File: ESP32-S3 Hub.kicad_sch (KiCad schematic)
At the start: 21 parts, among them U1 ESP32-S3 FN8, Y1 ABM11-40.000MHZ-B1U-T3, 10ppm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

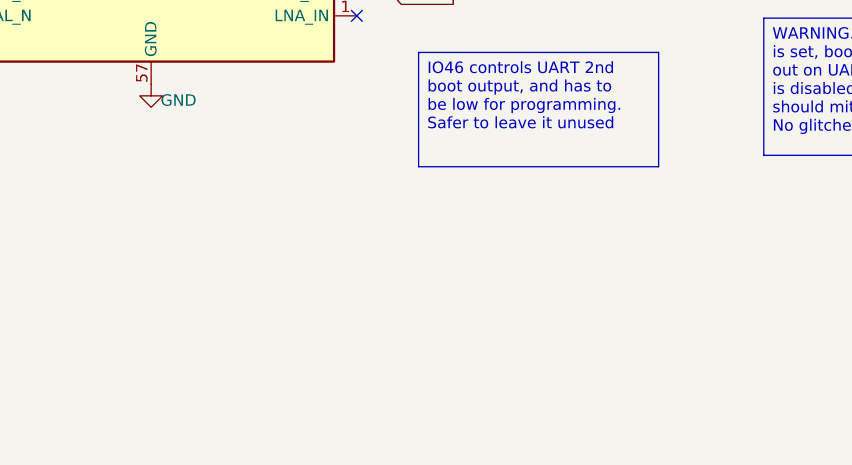
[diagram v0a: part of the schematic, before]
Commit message: Fixed typos with ADC-4 pins, split a few circuits
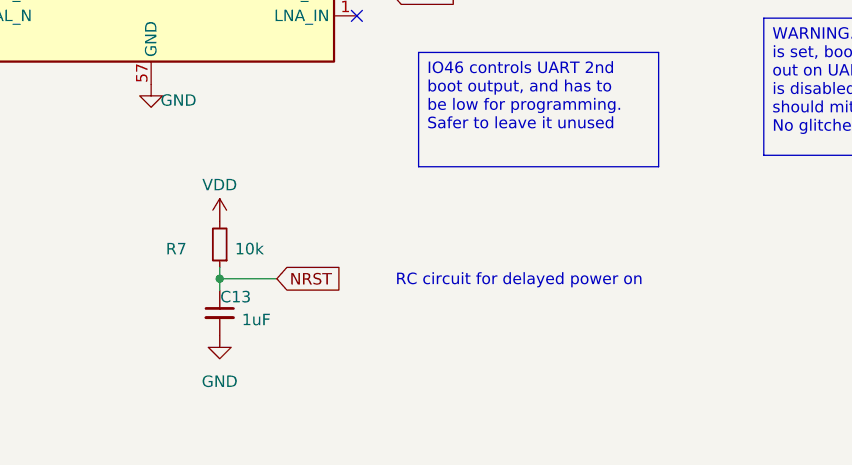
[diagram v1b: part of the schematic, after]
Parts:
- added C13: 1uF, Capacitor_SMD:C_0402_1005Metric, symbol Device:C_Small
- added R7: 10k, Resistor_SMD:R_0402_1005Metric, symbol Device:R_Small
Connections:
- net GND: now also C13.2
- net NRST: now also C13.1, R7.1
- net VDD: now also R7.2
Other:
- note added: "RC circuit for delayed power on"

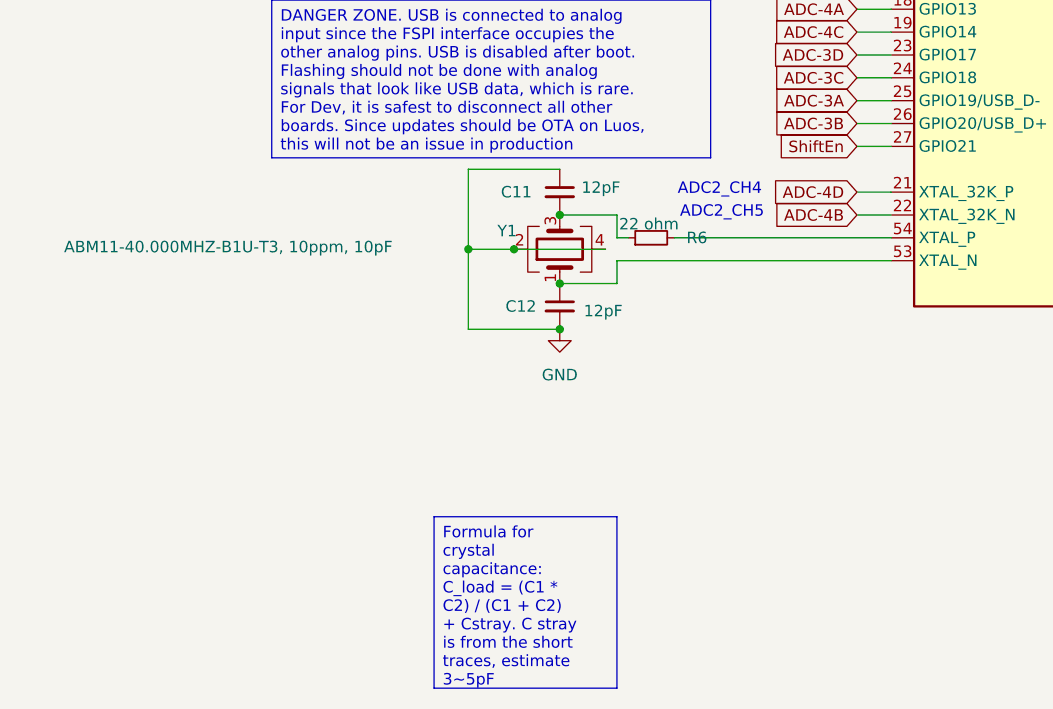
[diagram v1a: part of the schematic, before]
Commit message: Changed clock schematic layout
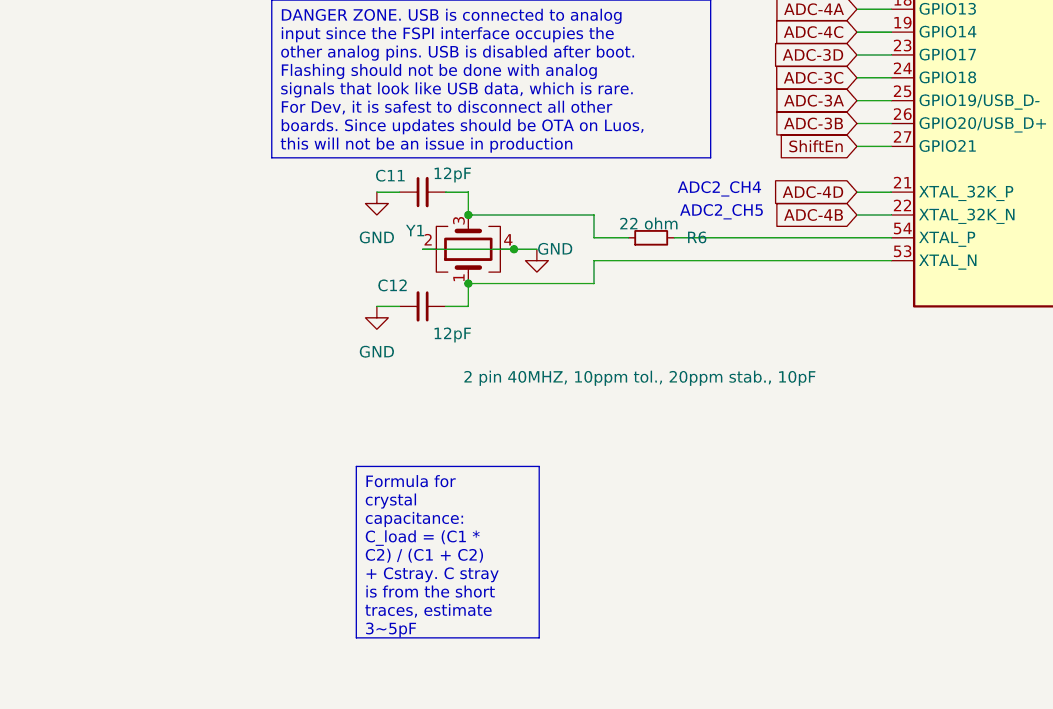
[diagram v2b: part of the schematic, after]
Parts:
- Y1: value ABM11-40.000MHZ-B1U-T3, 10ppm, 10pF -> 2 pin 40MHZ, 10ppm tol., 20ppm stab., 10pF
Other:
- moved on the sheet: C11, C12, Y1

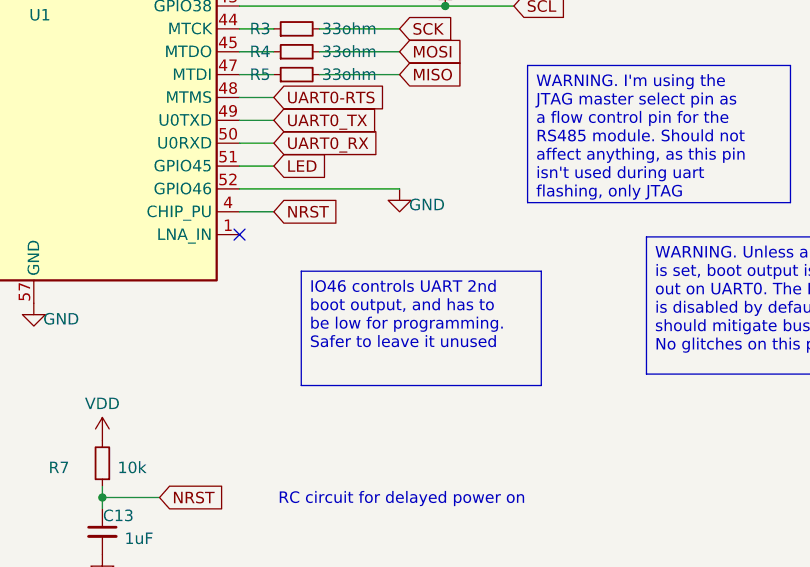
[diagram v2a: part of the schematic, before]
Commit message: Changed configurable resistor pin in schematic
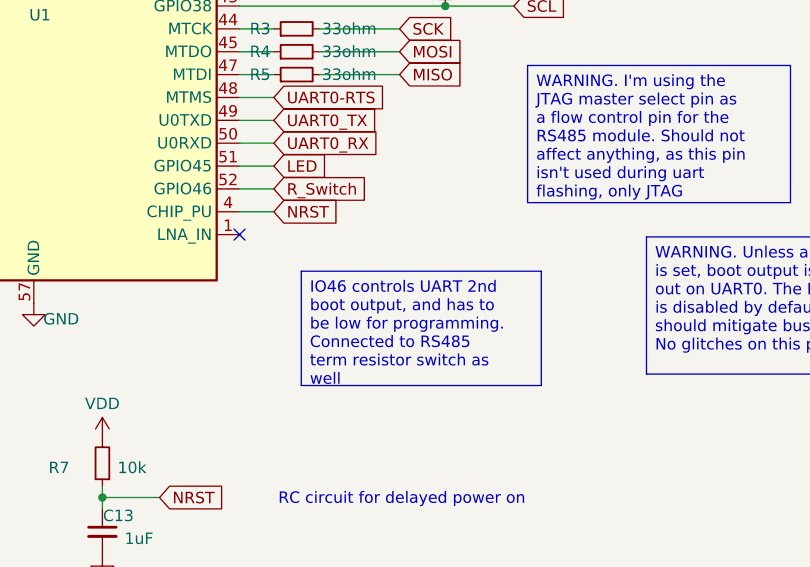
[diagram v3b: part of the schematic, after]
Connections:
- net GND: no longer U1.52 (GPIO46)
- new net R_Switch: U1.52 (GPIO46)
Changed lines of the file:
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@@
 		)
 	)
-	(text_box "IO46 controls UART 2nd boot output, and has to be low for programming. Safer to leave it unused"
+	(text_box "IO46 controls UART 2nd boot output, and has to be low for programming. Connected to RS485 term resistor switch as well"
 		(exclude_from_sim no)
 		(at 174.498 127.254 0)
@@
 	(wire
 		(pts
-			(xy 167.64 118.11) (xy 185.42 118.11)
+			(xy 167.64 118.11) (xy 171.45 118.11)
 		)
 		(stroke
@@
 		)
 	)
+	(global_label "R_Switch"
+		(shape input)
+		(at 171.45 118.11 0)
+		(fields_autoplaced yes)
+		(effects
+			(font
+				(size 1.27 1.27)
+			)
+			(justify left)
+		)
+		(property "Intersheetrefs" "${INTERSHEET_REFS}"
+			(at 182.7809 118.11 0)
+			(effects
+				(font
+					(size 1.27 1.27)
+				)
+				(justify left)
+				(hide yes)
+			)
+		)
+	)
 	(global_label "CS-3"
 		(shape input)
@@
 					(unit 1)
 				)
-			)
-		)
-	)
-	(symbol
-		(lib_id "power:GND")
-		(at 185.42 118.11 0)
-		(unit 1)
-		(exclude_from_sim no)
-		(in_bom yes)
-		(on_board yes)
-		(dnp no)
-		(property "Reference" "#PWR043"
-			(at 185.42 124.46 0)
-			(effects
-				(font
-					(size 1.27 1.27)
-				)
-				(hide yes)
-			)
-		)
-		(property "Value" "GND"
-			(at 188.468 119.888 0)
-			(effects
-				(font
-					(size 1.27 1.27)
-				)
-			)
-		)
-		(property "Footprint" ""
-			(at 185.42 118.11 0)
-			(effects
-				(font
-					(size 1.27 1.27)
-				)
-				(hide yes)
-			)
-		)
-		(property "Datasheet" ""
-			(at 185.42 118.11 0)
-			(effects
-				(font
-					(size 1.27 1.27)
-				)
-				(hide yes)
-			)
-		)
-		(property "Description" "Power symbol creates a global label with name \"GND\" , ground"
-			(at 185.42 118.11 0)
-			(effects
-				(font
-					(size 1.27 1.27)
-				)
-				(hide yes)
-			)
-		)
-		(pin "1"
-		)
-		(instances
-			(project "ESP32-S3 Hub"
-				(path "/a8c80fba-3bca-4358-b5bb-9ebf9383c658"
-					(reference "#PWR043")
-					(unit 1)
-				)

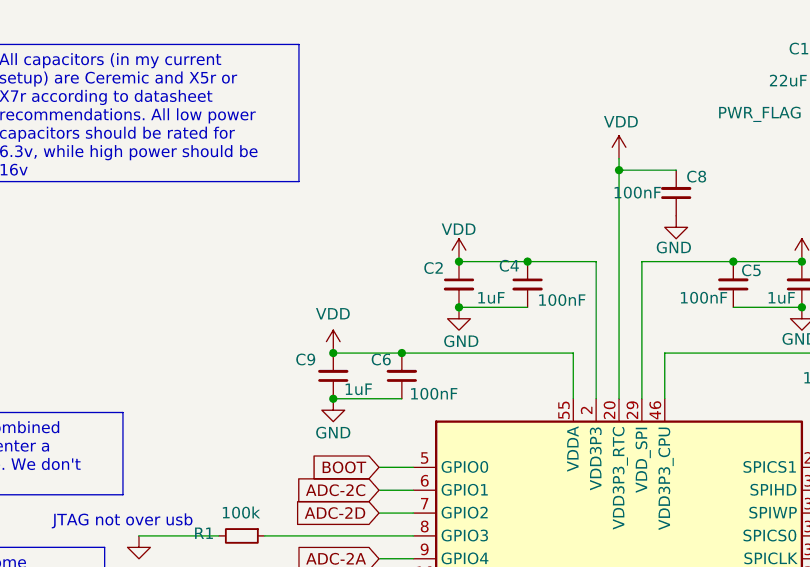
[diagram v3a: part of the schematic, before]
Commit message: Added 1 more bulk decop capacitor
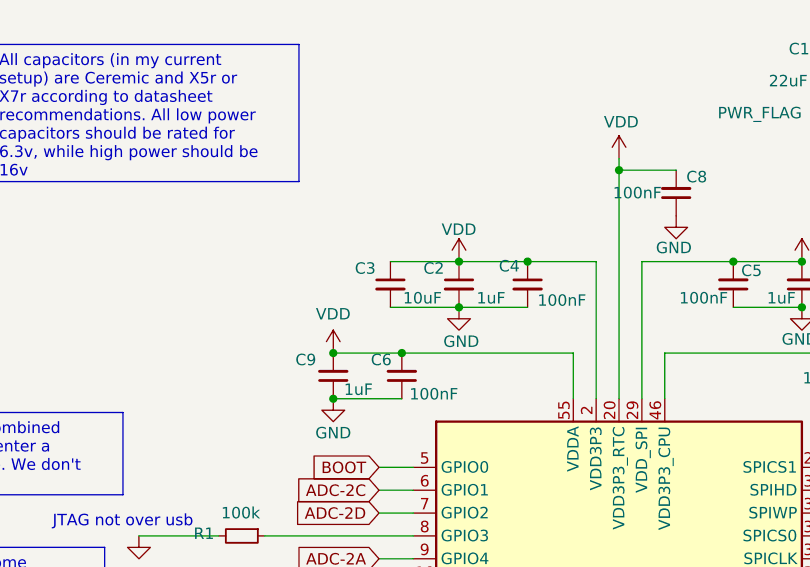
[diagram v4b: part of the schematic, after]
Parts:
- added C3: 10uF, Capacitor_SMD:C_0402_1005Metric, symbol Device:C_Small
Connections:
- net GND: now also C3.2
- net VDD: now also C3.1
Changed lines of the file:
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@@
+	(wire
+		(pts
+			(xy 119.38 44.45) (xy 127 44.45)
+		)
+		(stroke
+			(width 0)
+			(type default)
+		)
+	)
 	(wire
 		(pts
@@
 		(pts
 			(xy 171.45 22.86) (xy 173.99 22.86)
+		)
+		(stroke
+			(width 0)
+			(type default)
+		)
+	)
+	(wire
+		(pts
+			(xy 119.38 39.37) (xy 127 39.37)
 		)
 		(stroke
@@
 					(unit 1)
 				)
+			)
+		)
+	)
+	(symbol
+		(lib_id "Device:C_Small")
+		(at 119.38 41.91 0)
+		(unit 1)
+		(exclude_from_sim no)
+		(in_bom yes)
+		(on_board yes)
+		(dnp no)
+		(property "Reference" "C3"
+			(at 116.586 40.132 0)
+			(effects
+				(font
+					(size 1.27 1.27)
+				)
+			)
+		)
+		(property "Value" "10uF"
+			(at 122.936 43.434 0)
+			(effects
+				(font
+					(size 1.27 1.27)
+				)
+			)
+		)
+		(property "Footprint" "Capacitor_SMD:C_0402_1005Metric"
+			(at 119.38 41.91 0)
+			(effects
+				(font
+					(size 1.27 1.27)
+				)
+				(hide yes)
+			)
+		)
+		(property "Datasheet" "~"
+			(at 119.38 41.91 0)
+			(effects
+				(font
+					(size 1.27 1.27)
+				)
+				(hide yes)
+			)
+		)
+		(property "Description" "Unpolarized capacitor, small symbol"
+			(at 119.38 41.91 0)
+			(effects
+				(font
+					(size 1.27 1.27)
+				)
+				(hide yes)
+			)
+		)
+		(property "LCSC" "C52923"
+			(at 121.92 42.672 0)
+			(effects
+				(font
+					(size 1.27 1.27)
+				)
+				(hide yes)
+			)
+		)
+		(pin "2"
+		)
+		(pin "1"
+		)
+		(instances
+			(project "ESP32-S3 Hub"
+				(path "/a8c80fba-3bca-4358-b5bb-9ebf9383c658"
+					(reference "C3")
+					(unit 1)
+				)

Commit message: Fixed BOM LCSC part numbers mostly
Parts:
- C3: LCSC C52923 -> C15525
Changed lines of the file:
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@@
 			)
 		)
-		(property "LCSC" "C52923"
+		(property "LCSC" "C15525"
 			(at 121.92 42.672 0)
 			(effects

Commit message: Fixed clock to be on top only, moved to 0201, separate clock signals
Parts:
- C11, C12: footprint Capacitor_SMD:C_0402_1005Metric -> Capacitor_SMD:C_0201_0603Metric; LCSC C1547 -> C384960
- R6: footprint Resistor_SMD:R_0402_1005Metric -> Resistor_SMD:R_0201_0603Metric; LCSC C25092 -> C155743
- Y1: footprint Crystal:Crystal_SMD_2016-4Pin_2.0x1.6mm -> custom_Crystal:Crystal_SMD_1612-4Pin_1.6x1.2mm; LCSC C648973 -> C49158191
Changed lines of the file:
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@@
 			)
 		)
-		(property "Footprint" "Crystal:Crystal_SMD_2016-4Pin_2.0x1.6mm"
+		(property "Footprint" "custom_Crystal:Crystal_SMD_1612-4Pin_1.6x1.2mm"
 			(at 74.93 121.92 0)
 			(effects
@@
 			)
 		)
-		(property "LCSC" "C648973"
+		(property "LCSC" "C49158191"
 			(at 76.2 122.428 0)
 			(effects
@@
 			)
 		)
-		(property "Footprint" "Capacitor_SMD:C_0402_1005Metric"
+		(property "Footprint" "Capacitor_SMD:C_0201_0603Metric"
 			(at 69.85 128.27 0)
 			(effects
@@
 			)
 		)
-		(property "LCSC" "C1547"
+		(property "LCSC" "C384960"
 			(at 68.834 128.016 0)
 			(effects
@@
 			)
 		)
-		(property "Footprint" "Resistor_SMD:R_0402_1005Metric"
+		(property "Footprint" "Resistor_SMD:R_0201_0603Metric"
 			(at 95.25 120.65 0)
 			(effects
@@
 			)
 		)
-		(property "LCSC" "C25092"
+		(property "LCSC" "C155743"
 			(at 93.218 121.92 0)
 			(effects
@@
 			)
 		)
-		(property "Footprint" "Capacitor_SMD:C_0402_1005Metric"
+		(property "Footprint" "Capacitor_SMD:C_0201_0603Metric"
 			(at 69.85 115.57 0)
 			(effects
@@
 			)
 		)
-		(property "LCSC" "C1547"
+		(property "LCSC" "C384960"
 			(at 70.866 115.824 0)
 			(effects

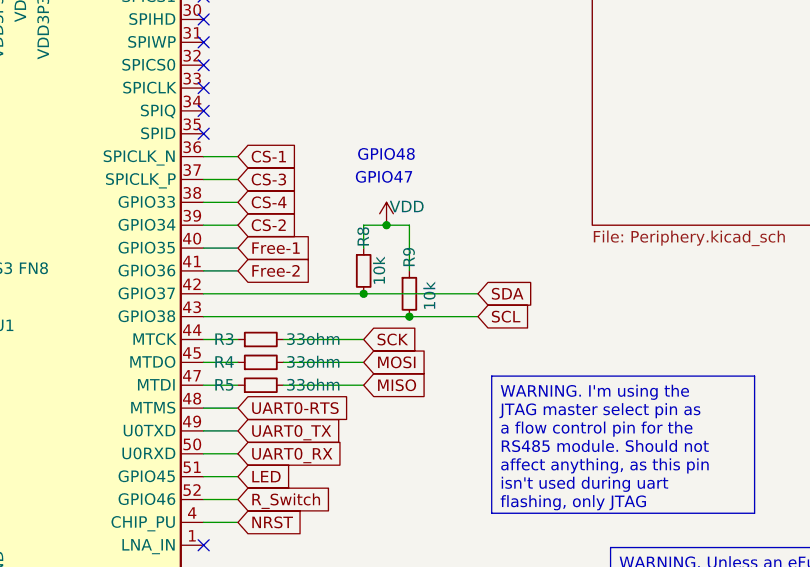
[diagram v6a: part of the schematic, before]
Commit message: Changed i2c resistors to be stronger
The distance is really short and I was only ever planning on having a few devices per hub, so strength is increased.
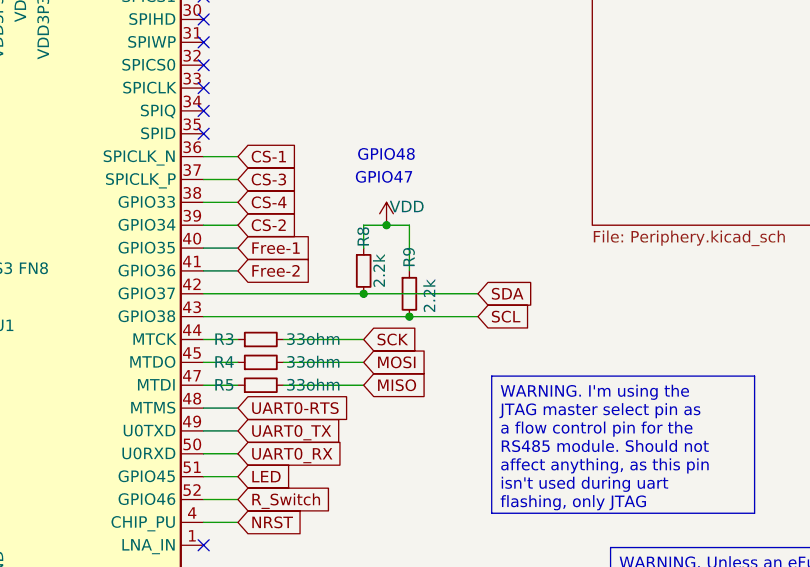
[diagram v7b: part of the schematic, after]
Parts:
- R8, R9: value 10k -> 2.2k; LCSC C25744 -> C25879
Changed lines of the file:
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@@
 			)
 		)
-		(property "Value" "10k"
+		(property "Value" "2.2k"
 			(at 187.198 92.71 90)
 			(effects
@@
 			)
 		)
-		(property "LCSC" "C25744"
+		(property "LCSC" "C25879"
 			(at 185.928 88.646 0)
 			(effects
@@
 			)
 		)
-		(property "Value" "10k"
+		(property "Value" "2.2k"
 			(at 192.786 95.504 90)
 			(effects
@@
 			)
 		)
-		(property "LCSC" "C25744"
+		(property "LCSC" "C25879"
 			(at 191.008 91.186 0)
 			(effects
